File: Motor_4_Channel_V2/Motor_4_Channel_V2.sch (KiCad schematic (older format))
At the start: 60 parts, among them J1 Conn_01x02_Male, J10 Conn_01x02_Male, J11 Conn_01x10_Male, J2 Conn_01x02_Male, J3 Conn_01x02_Male, J4 Conn_01x02_Male, J5 Conn_01x02_Male, J6 Conn_01x02_Male, J7 Conn_01x02_Male, J8 Conn_01x10_Male, J9 Conn_01x02_Male, P1 Pad, P10 Pad, P11 Pad, P12 Pad, P2 Pad, P3 Pad, P4 Pad, P5 Pad, P6 Pad, P7 Pad, P8 Pad, P9 Pad, SW1 SW_SPST, U1 SN74LVC1G139DCUR, U10 NC7WZ14P6XCT-ND, U11 MSP430G2553_LP, U2 SN74LVC1G139DCUR, U3 UA78M05IDCY, U4 UA78M33QDCYRG4Q1, U5 NC7WZ14P6XCT-ND, U6 NC7WZ14P6XCT-ND, U7 SN74LVC1G139DCUR, U8 SN74LVC1G139DCUR, U9 NC7WZ14P6XCT-ND

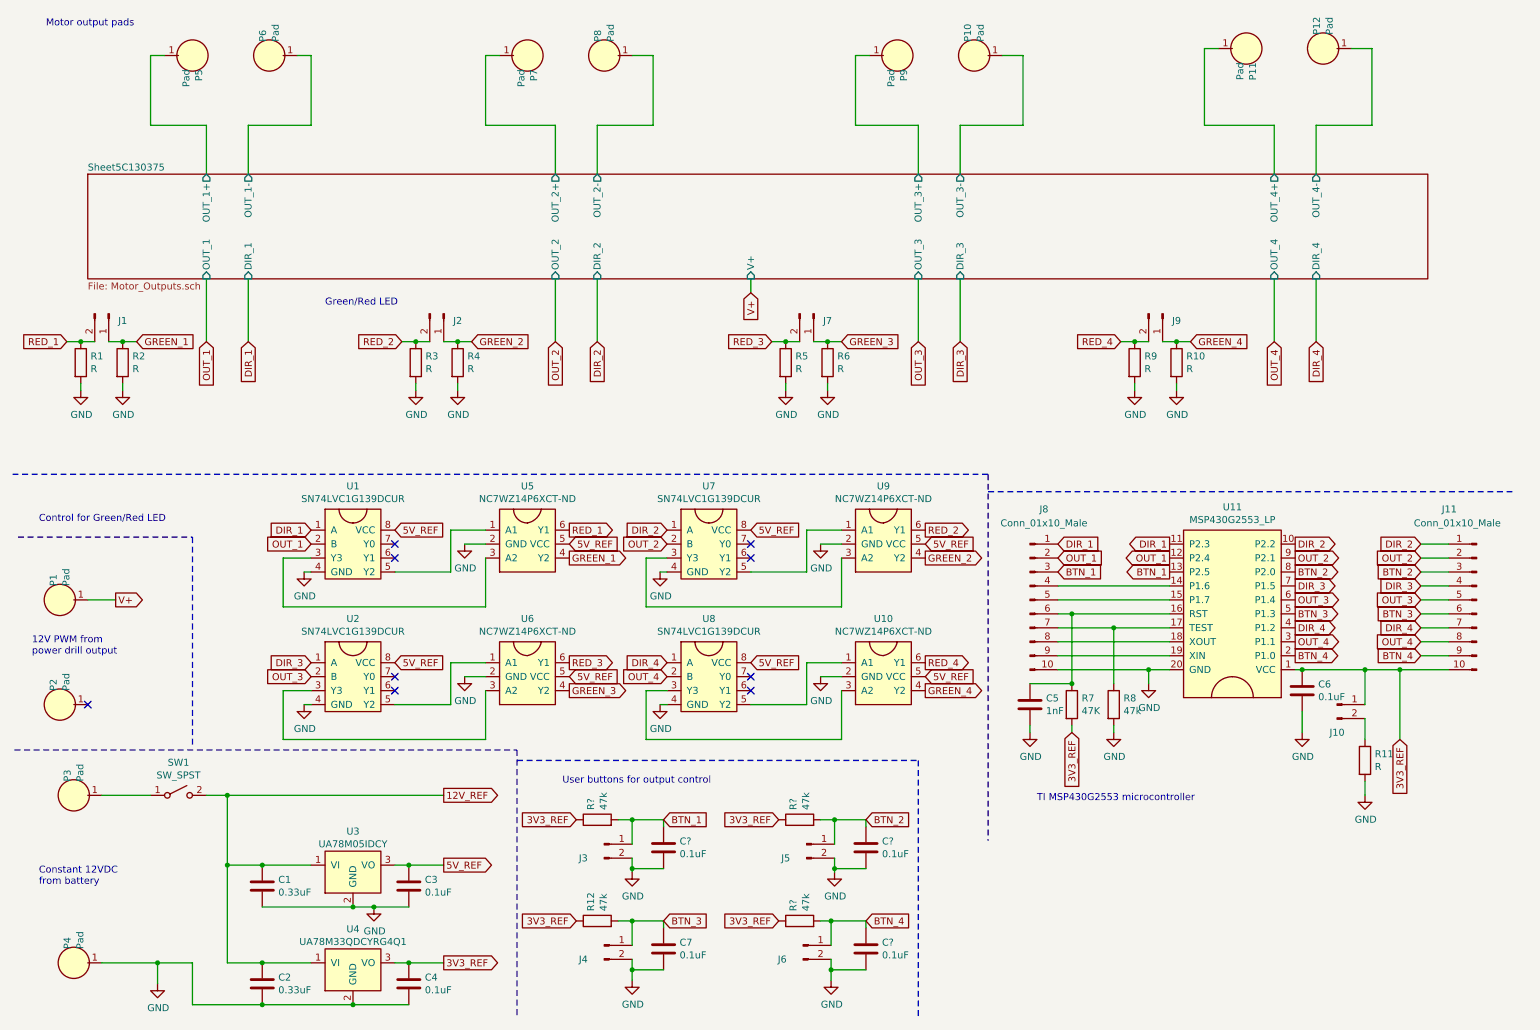
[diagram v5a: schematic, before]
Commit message: Changed output Red/Green LED circuit to charlieplexing design.
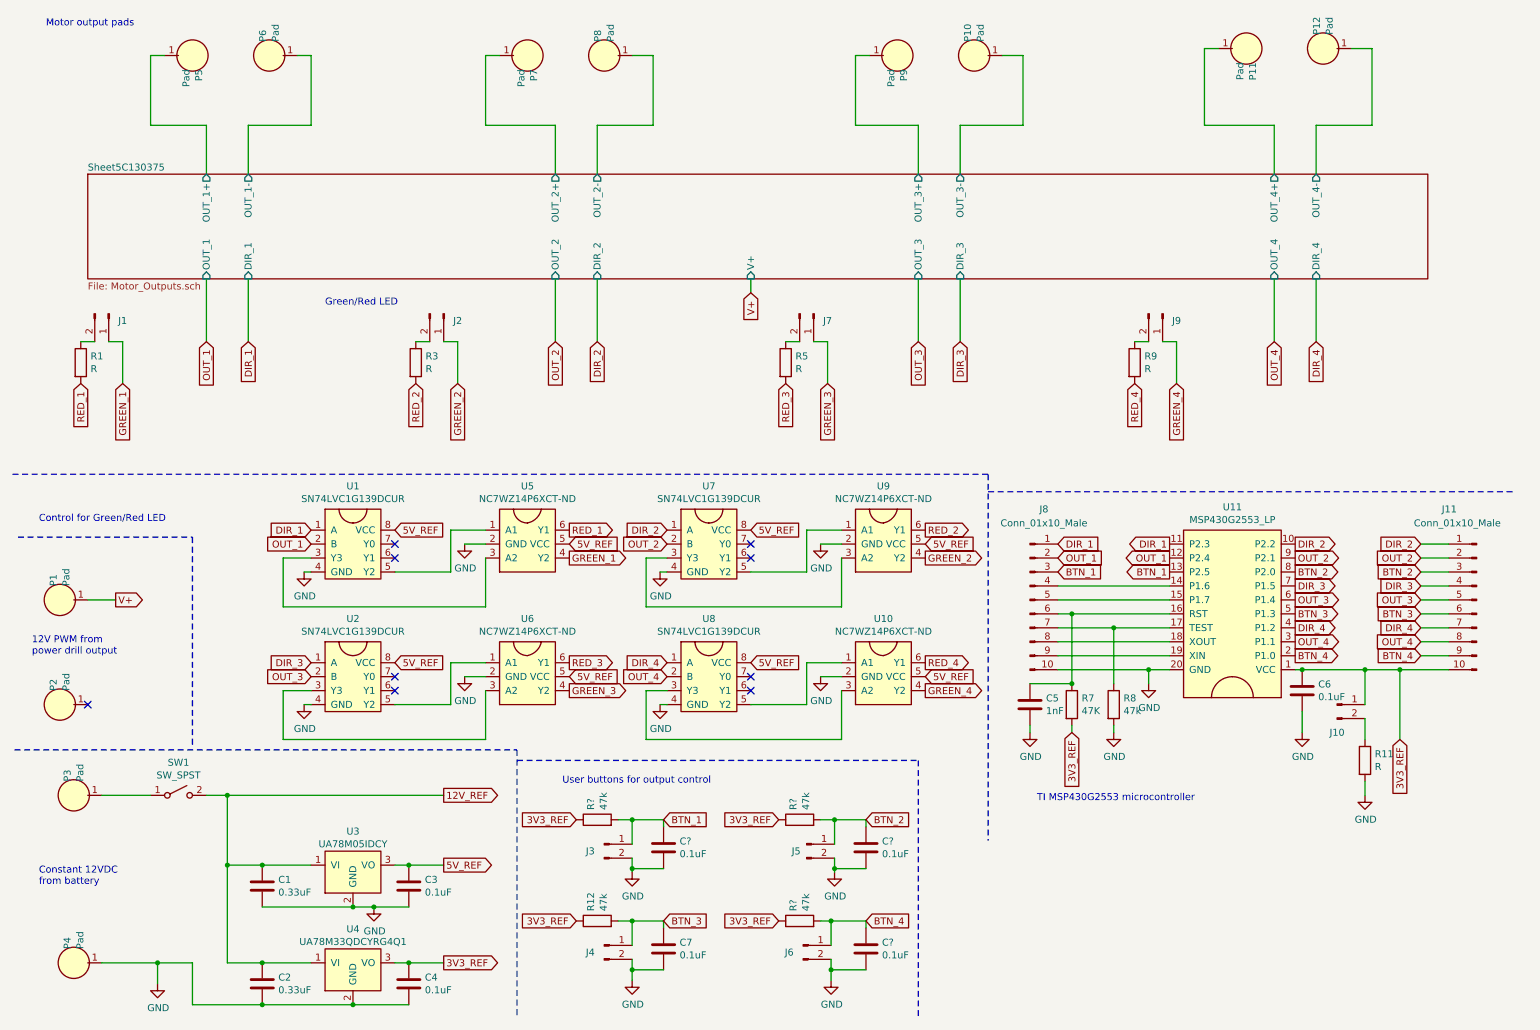
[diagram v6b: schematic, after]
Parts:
- removed R10, R2, R4, R6: R, Resistor_SMD:R_0603_1608Metric_Pad1.05x0.95mm_HandSolder, symbol Device:R
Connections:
- net GND: no longer R1.2, R3.2, R5.2, R9.2
- net RED_1: now also R1.2; no longer J1.2 (Pin_2), R1.1
- net RED_2: now also R3.2; no longer J2.2 (Pin_2), R3.1
- net RED_3: now also R5.2; no longer J7.2 (Pin_2), R5.1
- net RED_4: now also R9.2; no longer J9.2 (Pin_2), R9.1
- new net: J9.2 (Pin_2), R9.1
- new net: J7.2 (Pin_2), R5.1
- new net: J2.2 (Pin_2), R3.1
- new net: J1.2 (Pin_2), R1.1
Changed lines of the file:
@@
 U 1 1 5C0D215D
 P 4700 6550
-F 0 "J3" H 4550 6450 50  0000 C CNN
+F 0 "J3" H 4600 6500 50  0000 C CNN
 F 1 "Conn_01x02_Male" H 4500 6350 50  0001 C CNN
 F 2 "Connector_PinHeader_2.54mm:PinHeader_1x02_P2.54mm_Vertical_SMD_Pin1Left" H 4700 6550 50  0001 C CNN
@@
 U 1 1 5C0D2243
 P 6150 6550
-F 0 "J5" H 6000 6450 50  0000 C CNN
+F 0 "J5" H 6075 6500 50  0000 C CNN
 F 1 "Conn_01x02_Male" H 5950 6350 50  0001 C CNN
 F 2 "Connector_PinHeader_2.54mm:PinHeader_1x02_P2.54mm_Vertical_SMD_Pin1Left" H 6150 6550 50  0001 C CNN
@@
 U 1 1 5C0D22BD
 P 4700 7275
-F 0 "J4" H 4550 7175 50  0000 C CNN
+F 0 "J4" H 4600 7225 50  0000 C CNN
 F 1 "Conn_01x02_Male" H 4500 7075 50  0001 C CNN
 F 2 "Connector_PinHeader_2.54mm:PinHeader_1x02_P2.54mm_Vertical_SMD_Pin1Left" H 4700 7275 50  0001 C CNN
@@
 U 1 1 5C0D232B
 P 6125 7275
-F 0 "J6" H 5975 7175 50  0000 C CNN
+F 0 "J6" H 6025 7225 50  0000 C CNN
 F 1 "Conn_01x02_Male" H 5925 7075 50  0001 C CNN
 F 2 "Connector_PinHeader_2.54mm:PinHeader_1x02_P2.54mm_Vertical_SMD_Pin1Left" H 6125 7275 50  0001 C CNN
@@
 	1    0    0    -1
 $EndComp
-$Comp
-L Device:R R10
-U 1 1 5BF9B2EE
-P 8800 3100
-F 0 "R10" H 8870 3146 50  0000 L CNN
-F 1 "R" H 8870 3055 50  0000 L CNN
-F 2 "Resistor_SMD:R_0603_1608Metric_Pad1.05x0.95mm_HandSolder" V 8730 3100 50  0001 C CNN
-F 3 "~" H 8800 3100 50  0001 C CNN
-	1    8800 3100
-	1    0    0    -1
-$EndComp
-$Comp
-L power:GND #PWR026
-U 1 1 5BF9B2F5
-P 8800 3300
-F 0 "#PWR026" H 8800 3050 50  0001 C CNN
-F 1 "GND" H 8805 3127 50  0000 C CNN
-F 2 "" H 8800 3300 50  0001 C CNN
-F 3 "" H 8800 3300 50  0001 C CNN
-	1    8800 3300
-	1    0    0    -1
-$EndComp
 Text GLabel 4450 4300 2    50   Output ~ 0
 RED_1
@@
 Text GLabel 7000 5450 2    50   Output ~ 0
 GREEN_4
-Text GLabel 8400 2950 0    50   Input ~ 0
+Text GLabel 8500 3250 3    50   Input ~ 0
 RED_4
-Text GLabel 8900 2950 2    50   Input ~ 0
+Text GLabel 8800 3250 3    50   Input ~ 0
 GREEN_4
 Wire Notes Line
@@
 	0    1    1    0
 $EndComp
-$Comp
-L power:GND #PWR024
-U 1 1 5BF718D9
-P 8500 3300
-F 0 "#PWR024" H 8500 3050 50  0001 C CNN
-F 1 "GND" H 8505 3127 50  0000 C CNN
-F 2 "" H 8500 3300 50  0001 C CNN
-F 3 "" H 8500 3300 50  0001 C CNN
-	1    8500 3300
-	1    0    0    -1
-$EndComp
-Wire Wire Line
-	8400 2950 8500 2950
 Wire Wire Line
 	8700 2950 8800 2950
-Connection ~ 8500 2950
 Wire Wire Line
 	8500 2950 8600 2950
-Wire Wire Line
-	8800 2950 8900 2950
-Connection ~ 8800 2950
-Wire Wire Line
-	8500 3300 8500 3250
-Wire Wire Line
-	8800 3300 8800 3250
 $Comp
 L Device:R R5
@@
 	1    0    0    -1
 $EndComp
-$Comp
-L Device:R R6
-U 1 1 5BFAF9C5
-P 6300 3100
-F 0 "R6" H 6370 3146 50  0000 L CNN
-F 1 "R" H 6370 3055 50  0000 L CNN
-F 2 "Resistor_SMD:R_0603_1608Metric_Pad1.05x0.95mm_HandSolder" V 6230 3100 50  0001 C CNN
-F 3 "~" H 6300 3100 50  0001 C CNN
-	1    6300 3100
-	1    0    0    -1
-$EndComp
-$Comp
-L power:GND #PWR019
-U 1 1 5BFAF9CC
-P 6300 3300
-F 0 "#PWR019" H 6300 3050 50  0001 C CNN
-F 1 "GND" H 6305 3127 50  0000 C CNN
-F 2 "" H 6300 3300 50  0001 C CNN
-F 3 "" H 6300 3300 50  0001 C CNN
-	1    6300 3300
-	1    0    0    -1
-$EndComp
-Text GLabel 5900 2950 0    50   Input ~ 0
+Text GLabel 6000 3250 3    50   Input ~ 0
 RED_3
-Text GLabel 6400 2950 2    50   Input ~ 0
+Text GLabel 6300 3250 3    50   Input ~ 0
 GREEN_3
 $Comp
@@
 	0    1    1    0
 $EndComp
-$Comp
-L power:GND #PWR016
-U 1 1 5BFAF9DB
-P 6000 3300
-F 0 "#PWR016" H 6000 3050 50  0001 C CNN
-F 1 "GND" H 6005 3127 50  0000 C CNN
-F 2 "" H 6000 3300 50  0001 C CNN
-F 3 "" H 6000 3300 50  0001 C CNN
-	1    6000 3300
-	1    0    0    -1
-$EndComp
-Wire Wire Line
-	5900 2950 6000 2950
-Wire Wire Line
-	6200 2950 6300 2950
-Connection ~ 6000 2950
 Wire Wire Line
 	6000 2950 6100 2950
-Wire Wire Line
-	6300 2950 6400 2950
-Connection ~ 6300 2950
-Wire Wire Line
-	6000 3300 6000 3250
-Wire Wire Line
-	6300 3300 6300 3250
 $Comp
 L Device:R R3
@@
 	1    0    0    -1
 $EndComp
-$Comp
-L Device:R R4
-U 1 1 5BFB5C39
-P 3650 3100
-F 0 "R4" H 3720 3146 50  0000 L CNN
-F 1 "R" H 3720 3055 50  0000 L CNN
-F 2 "Resistor_SMD:R_0603_1608Metric_Pad1.05x0.95mm_HandSolder" V 3580 3100 50  0001 C CNN
-F 3 "~" H 3650 3100 50  0001 C CNN
-	1    3650 3100
-	1    0    0    -1
-$EndComp
-$Comp
-L power:GND #PWR09
-U 1 1 5BFB5C40
-P 3650 3300
-F 0 "#PWR09" H 3650 3050 50  0001 C CNN
-F 1 "GND" H 3655 3127 50  0000 C CNN
-F 2 "" H 3650 3300 50  0001 C CNN
-F 3 "" H 3650 3300 50  0001 C CNN
-	1    3650 3300
-	1    0    0    -1
-$EndComp
-Text GLabel 3250 2950 0    50   Input ~ 0
+Text GLabel 3350 3250 3    50   Input ~ 0
 RED_2
-Text GLabel 3750 2950 2    50   Input ~ 0
+Text GLabel 3650 3250 3    50   Input ~ 0
 GREEN_2
 $Comp
@@
 	0    1    1    0
 $EndComp
-$Comp
-L power:GND #PWR08
-U 1 1 5BFB5C4F
-P 3350 3300
-F 0 "#PWR08" H 3350 3050 50  0001 C CNN
-F 1 "GND" H 3355 3127 50  0000 C CNN
-F 2 "" H 3350 3300 50  0001 C CNN
-F 3 "" H 3350 3300 50  0001 C CNN
-	1    3350 3300
-	1    0    0    -1
-$EndComp
-Wire Wire Line
-	3250 2950 3350 2950
-Wire Wire Line
-	3550 2950 3650 2950
-Connection ~ 3350 2950
 Wire Wire Line
 	3350 2950 3450 2950
-Wire Wire Line
-	3650 2950 3750 2950
-Connection ~ 3650 2950
-Wire Wire Line
-	3350 3300 3350 3250
-Wire Wire Line
-	3650 3300 3650 3250
 $Comp
 L Device:R R1
@@
 	1    0    0    -1
 $EndComp
-$Comp
-L Device:R R2
-U 1 1 5BFBC837
-P 1250 3100
-F 0 "R2" H 1320 3146 50  0000 L CNN
-F 1 "R" H 1320 3055 50  0000 L CNN
-F 2 "Resistor_SMD:R_0603_1608Metric_Pad1.05x0.95mm_HandSolder" V 1180 3100 50  0001 C CNN
-F 3 "~" H 1250 3100 50  0001 C CNN
-	1    1250 3100
-	1    0    0    -1
-$EndComp
-$Comp
-L power:GND #PWR02
-U 1 1 5BFBC83E
-P 1250 3300
-F 0 "#PWR02" H 1250 3050 50  0001 C CNN
-F 1 "GND" H 1255 3127 50  0000 C CNN
-F 2 "" H 1250 3300 50  0001 C CNN
-F 3 "" H 1250 3300 50  0001 C CNN
-	1    1250 3300
-	1    0    0    -1
-$EndComp
-Text GLabel 850  2950 0    50   Input ~ 0
+Text GLabel 950  3250 3    50   Input ~ 0
 RED_1
-Text GLabel 1350 2950 2    50   Input ~ 0
+Text GLabel 1250 3250 3    50   Input ~ 0
 GREEN_1
 $Comp
@@
 	0    1    1    0
 $EndComp
-$Comp
-L power:GND #PWR01
-U 1 1 5BFBC84D
-P 950 3300
-F 0 "#PWR01" H 950 3050 50  0001 C CNN
-F 1 "GND" H 955 3127 50  0000 C CNN
-F 2 "" H 950 3300 50  0001 C CNN
-F 3 "" H 950 3300 50  0001 C CNN
-	1    950  3300
-	1    0    0    -1
-$EndComp
-Wire Wire Line
-	850  2950 950  2950
-Wire Wire Line
-	1150 2950 1250 2950
-Connection ~ 950  2950
 Wire Wire Line
 	950  2950 1050 2950
-Wire Wire Line
-	1250 2950 1350 2950
-Connection ~ 1250 2950
-Wire Wire Line
-	950  3300 950  3250
-Wire Wire Line
-	1250 3300 1250 3250
 $Comp
 L Device:R R12
@@
 Wire Wire Line
 	10400 5300 10400 5800
+Wire Wire Line
+	1150 2950 1250 2950
+Wire Wire Line
+	1250 2950 1250 3250
+Wire Wire Line
+	3550 2950 3650 2950
+Wire Wire Line
+	3650 2950 3650 3250
+Wire Wire Line
+	6200 2950 6300 2950
+Wire Wire Line
+	6300 2950 6300 3250
+Wire Wire Line
+	8800 2950 8800 3250
 $EndSCHEMATC

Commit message: Misc. changes to Motor PCB.
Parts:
- gave numbers to parts that had none: 6
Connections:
- net Sheet5C130375/OUT_1+: now also P6.1; no longer P5.1
- net Sheet5C130375/OUT_1-: now also P5.1; no longer P6.1
- net Sheet5C130375/OUT_2+: now also P8.1; no longer P7.1
- net Sheet5C130375/OUT_2-: now also P7.1; no longer P8.1
- net Sheet5C130375/OUT_3+: now also P10.1; no longer P9.1
- net Sheet5C130375/OUT_3-: now also P9.1; no longer P10.1
- net Sheet5C130375/OUT_4+: now also P12.1; no longer P11.1
- net Sheet5C130375/OUT_4-: now also P11.1; no longer P12.1
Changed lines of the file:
@@
 F0 "Sheet5C130375" 50
 F1 "Motor_Outputs.sch" 50
-F2 "OUT_1+" O T 1850 1750 50
-F3 "OUT_1-" O T 2150 1750 50
-F4 "OUT_2+" O T 4350 1750 50
-F5 "OUT_2-" O T 4650 1750 50
-F6 "OUT_3+" O T 6950 1750 50
-F7 "OUT_4+" O T 9500 1750 50
-F8 "OUT_4-" O T 9800 1750 50
+F2 "OUT_1+" O T 2150 1750 50
+F3 "OUT_1-" O T 1850 1750 50
+F4 "OUT_2+" O T 4650 1750 50
+F5 "OUT_2-" O T 4350 1750 50
+F6 "OUT_3+" O T 7250 1750 50
+F7 "OUT_4+" O T 9800 1750 50
+F8 "OUT_4-" O T 9500 1750 50
 F9 "DIR_1" I B 2150 2500 50
-F10 "OUT_3-" O T 7250 1750 50
+F10 "OUT_3-" O T 6950 1750 50
 F11 "DIR_2" I B 4650 2500 50
 F12 "DIR_3" I B 7250 2500 50
@@
 	4900 7450 4900 7525
 $Comp
-L Device:C C?
+L Device:C C10
 U 1 1 5C0417B7
 P 6575 7300
-F 0 "C?" H 6690 7346 50  0000 L CNN
+F 0 "C10" H 6690 7346 50  0000 L CNN
 F 1 "0.1uF" H 6690 7255 50  0000 L CNN
 F 2 "Capacitor_SMD:C_0603_1608Metric_Pad1.05x0.95mm_HandSolder" H 6613 7150 50  0001 C CNN
@@
 $EndComp
 $Comp
-L Device:R R?
+L Device:R R6
 U 1 1 5C041BDD
 P 6100 7100
-F 0 "R?" H 6170 7146 50  0000 L CNN
+F 0 "R6" H 6170 7146 50  0000 L CNN
 F 1 "47k" H 6170 7055 50  0000 L CNN
 F 2 "Resistor_SMD:R_0603_1608Metric_Pad1.05x0.95mm_HandSolder" V 6030 7100 50  0001 C CNN
@@
 	6325 7450 6325 7525
 $Comp
-L Device:C C?
+L Device:C C9
 U 1 1 5C067EF5
 P 6575 6575
-F 0 "C?" H 6690 6621 50  0000 L CNN
+F 0 "C9" H 6690 6621 50  0000 L CNN
 F 1 "0.1uF" H 6690 6530 50  0000 L CNN
 F 2 "Capacitor_SMD:C_0603_1608Metric_Pad1.05x0.95mm_HandSolder" H 6613 6425 50  0001 C CNN
@@
 $EndComp
 $Comp
-L Device:R R?
+L Device:R R4
 U 1 1 5C0681C8
 P 6100 6375
-F 0 "R?" H 6170 6421 50  0000 L CNN
+F 0 "R4" H 6170 6421 50  0000 L CNN
 F 1 "47k" H 6170 6330 50  0000 L CNN
 F 2 "Resistor_SMD:R_0603_1608Metric_Pad1.05x0.95mm_HandSolder" V 6030 6375 50  0001 C CNN
@@
 	6350 6725 6350 6750
 $Comp
-L Device:R R?
+L Device:R R2
 U 1 1 5C098E76
 P 4650 6375
-F 0 "R?" H 4720 6421 50  0000 L CNN
+F 0 "R2" H 4720 6421 50  0000 L CNN
 F 1 "47k" H 4720 6330 50  0000 L CNN
 F 2 "Resistor_SMD:R_0603_1608Metric_Pad1.05x0.95mm_HandSolder" V 4580 6375 50  0001 C CNN
@@
 $EndComp
 $Comp
-L Device:C C?
+L Device:C C8
 U 1 1 5C0990EE
 P 5125 6575
-F 0 "C?" H 5240 6621 50  0000 L CNN
+F 0 "C8" H 5240 6621 50  0000 L CNN
 F 1 "0.1uF" H 5240 6530 50  0000 L CNN
 F 2 "Capacitor_SMD:C_0603_1608Metric_Pad1.05x0.95mm_HandSolder" H 5163 6425 50  0001 C CNN
